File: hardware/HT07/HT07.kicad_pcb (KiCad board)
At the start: 2 copper layers, 54 x 54 mm, 35 parts, among them J30 Conn_02x04_Odd_Even, P1 Conn_01x01_MountingPin, P2 Conn_01x01_MountingPin, P3 Conn_01x01_MountingPin, P4 Conn_01x01_MountingPin, SW30 SW_Push, U1 HDC2021, U2 NT3H2111W0FTTJ, U3 MSP430FR2155TDBT, U4 SIP32431DR3-T1GE3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

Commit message: HT07R2 sent to manufacture at Eurocircuits
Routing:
- net GND: track 30.6 -> 33.4 mm

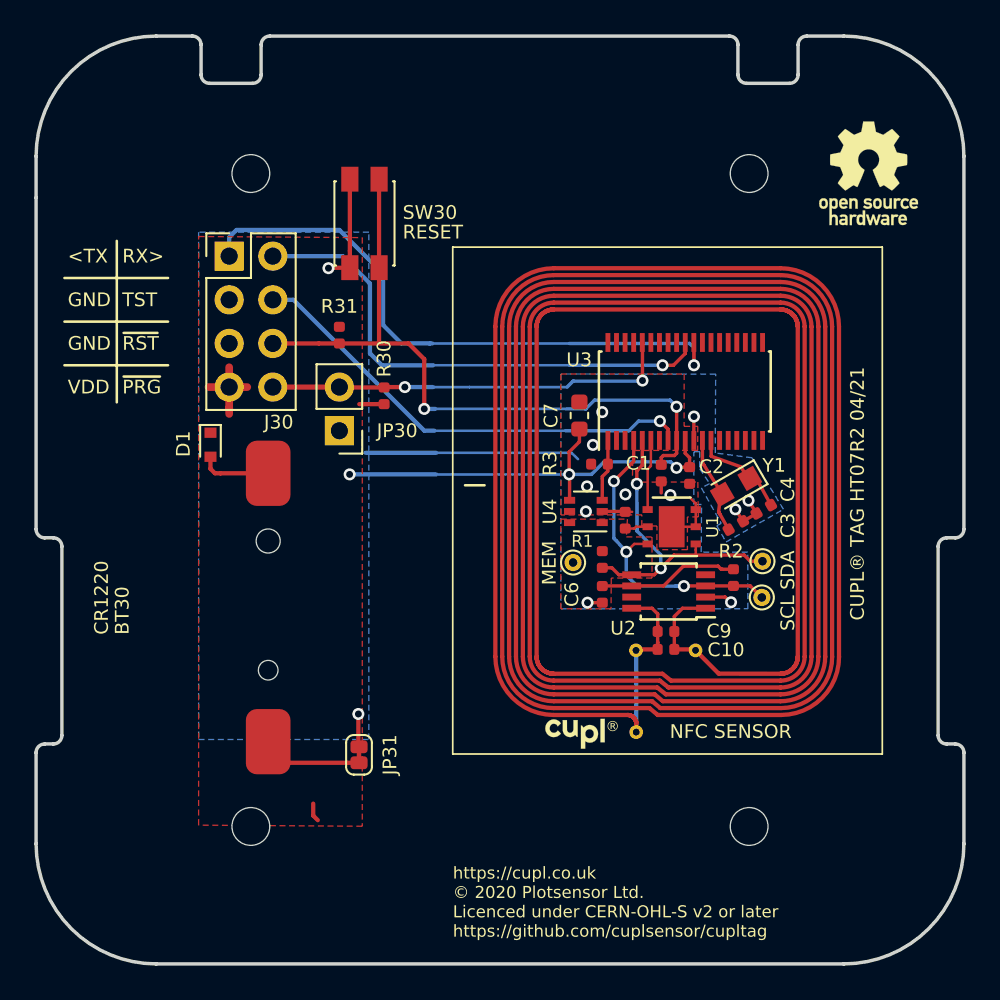
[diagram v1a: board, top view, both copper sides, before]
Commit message: Up-issued to Rev 3
This changes the humidity sensor to HDC2022 from HDC2021. Also adds alternate parts for the MSP430 and NT3H to the schematic.
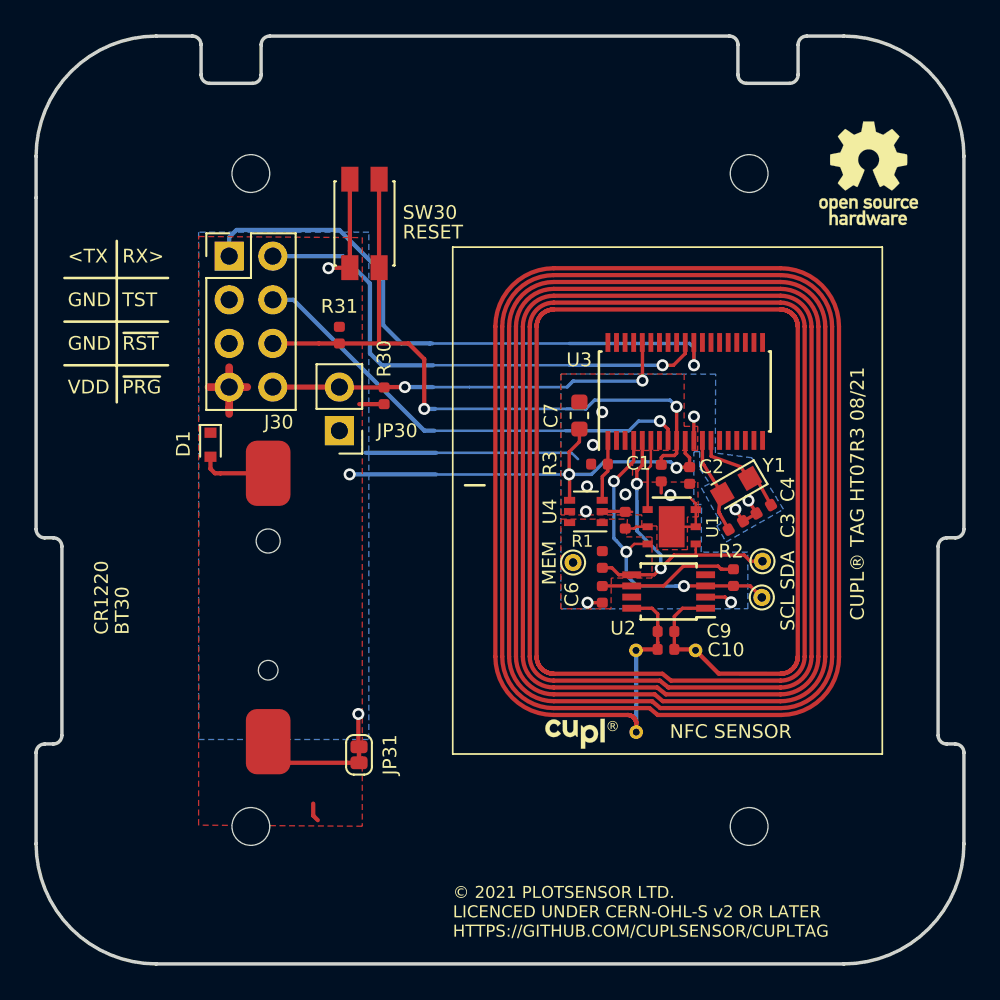
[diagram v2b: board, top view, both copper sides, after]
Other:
- board text added: "CUPL® TAG HT07R3 08/21"
- board text added: "© 2021 PLOTSENSOR LTD. LICENCED UNDER CERN-OHL-S v2 OR LATER HTTPS://GITHUB.COM/CUPLSENSOR/CUPLTAG"
- board text removed: "CUPL® TAG HT07R2 04/21"
- board text removed: "https://cupl.co.uk © 2020 Plotsensor Ltd. Licenced under CERN-OHL-S v2 or later https://github.com/cuplsensor/cupltag"
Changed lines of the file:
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@@
   )
   (setup
-    (last_trace_width 0.2)
+    (last_trace_width 0.15)
     (user_trace_width 0.15)
     (user_trace_width 0.2)
@@
     (effects (font (size 0.6 0.6) (thickness 0.11)) (justify left))
   )
-  (gr_text "https://cupl.co.uk\n© 2020 Plotsensor Ltd.\nLicenced under CERN-OHL-S v2 or later\nhttps://github.com/cuplsensor/cupltag" (at 107.5055 110.617) (layer F.SilkS)
+  (gr_text "\n© 2021 PLOTSENSOR LTD.\nLICENCED UNDER CERN-OHL-S v2 OR LATER\nHTTPS://GITHUB.COM/CUPLSENSOR/CUPLTAG" (at 107.5055 110.617) (layer F.SilkS)
     (effects (font (size 0.7 0.7) (thickness 0.12)) (justify left))
   )
@@
   (gr_line (start 92.350188 60.216393) (end 90.250188 60.216393) (layer Edge.Cuts) (width 0.2))
   (gr_line (start 108.212 86.36) (end 109.355 86.36) (layer F.SilkS) (width 0.15))
-  (gr_text "CUPL® TAG HT07R2 04/21" (at 131.056 94.234 90) (layer F.SilkS)
+  (gr_text "CUPL® TAG HT07R3 08/21" (at 131.056 94.234 90) (layer F.SilkS)
     (effects (font (size 0.8 0.8) (thickness 0.15)) (justify left))
   )

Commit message: Started to update documentation.
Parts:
- R3: value 47K -> 100K
- U1: value HDC2021 -> HDC2022DEPR
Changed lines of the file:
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@@
   )
   (setup
-    (last_trace_width 0.15)
+    (last_trace_width 0.25)
     (user_trace_width 0.15)
     (user_trace_width 0.2)
@@
       (effects (font (size 0.7 0.7) (thickness 0.15)))
     )
-    (fp_text value HDC2021 (at 0 2.725) (layer F.Fab) hide
+    (fp_text value HDC2022DEPR (at 0 2.725) (layer F.Fab) hide
       (effects (font (size 1 1) (thickness 0.15)))
     )
@@
       (effects (font (size 0.8 0.8) (thickness 0.15)))
     )
-    (fp_text value 47K (at 0 1.17) (layer F.Fab) hide
-      (effects (font (size 1 1) (thickness 0.15)))
-    )
+    (fp_text value 100K (at 0 1.17) (layer F.Fab) hide
+      (effects (font (size 1 1) (thickness 0.15)))
+    )
